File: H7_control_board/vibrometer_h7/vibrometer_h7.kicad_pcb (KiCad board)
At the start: 4 copper layers, 69.5 x 69.5 mm, 216 parts, among them J201 Conn_01x04_Socket, J204 TC2030-NL, J301 USB_C_Receptacle_USB2.0_16P, J501 debug_conn, J601 Conn_01x08_Socket, J701 Conn_01x08_Socket, J801 Conn_01x08_Socket, J901 PH-313D, Q1001 NMOS, Q1002 NMOS, Q1003 NMOS, Q201 BSS138, Q202 BSS138, Q203 BSS138, SW201 SW_Push, SW501 SW_Push, SW502 SW_Push, U201 STM32H723VGTx, U301 USBLC6-2SC6, U302 MT9700, U303 AMS1117-3V3, U901 RC4580, U902 TPA6111A2, Y201 24MHz

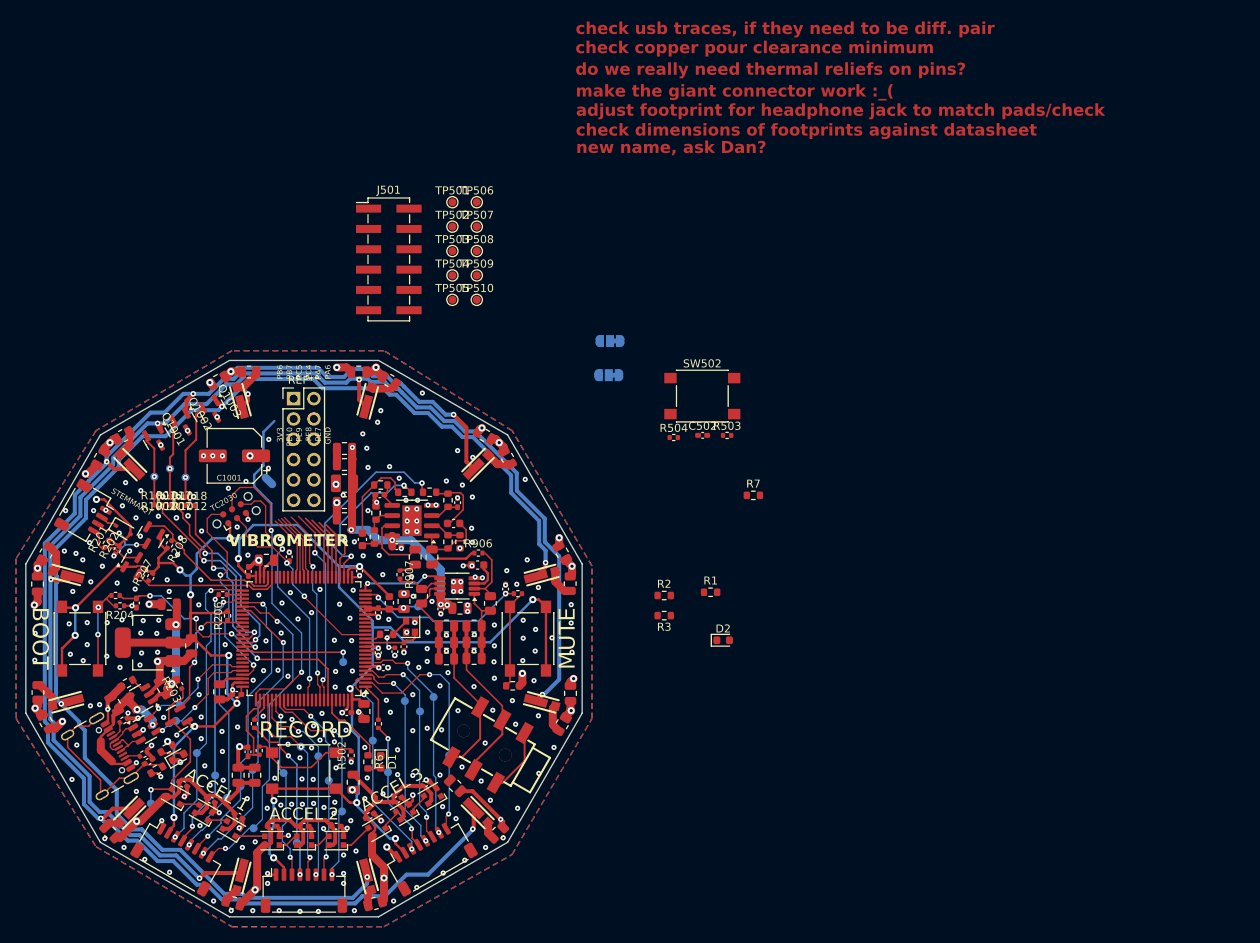
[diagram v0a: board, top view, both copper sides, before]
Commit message: some rerouting, cleaned up silkscreen
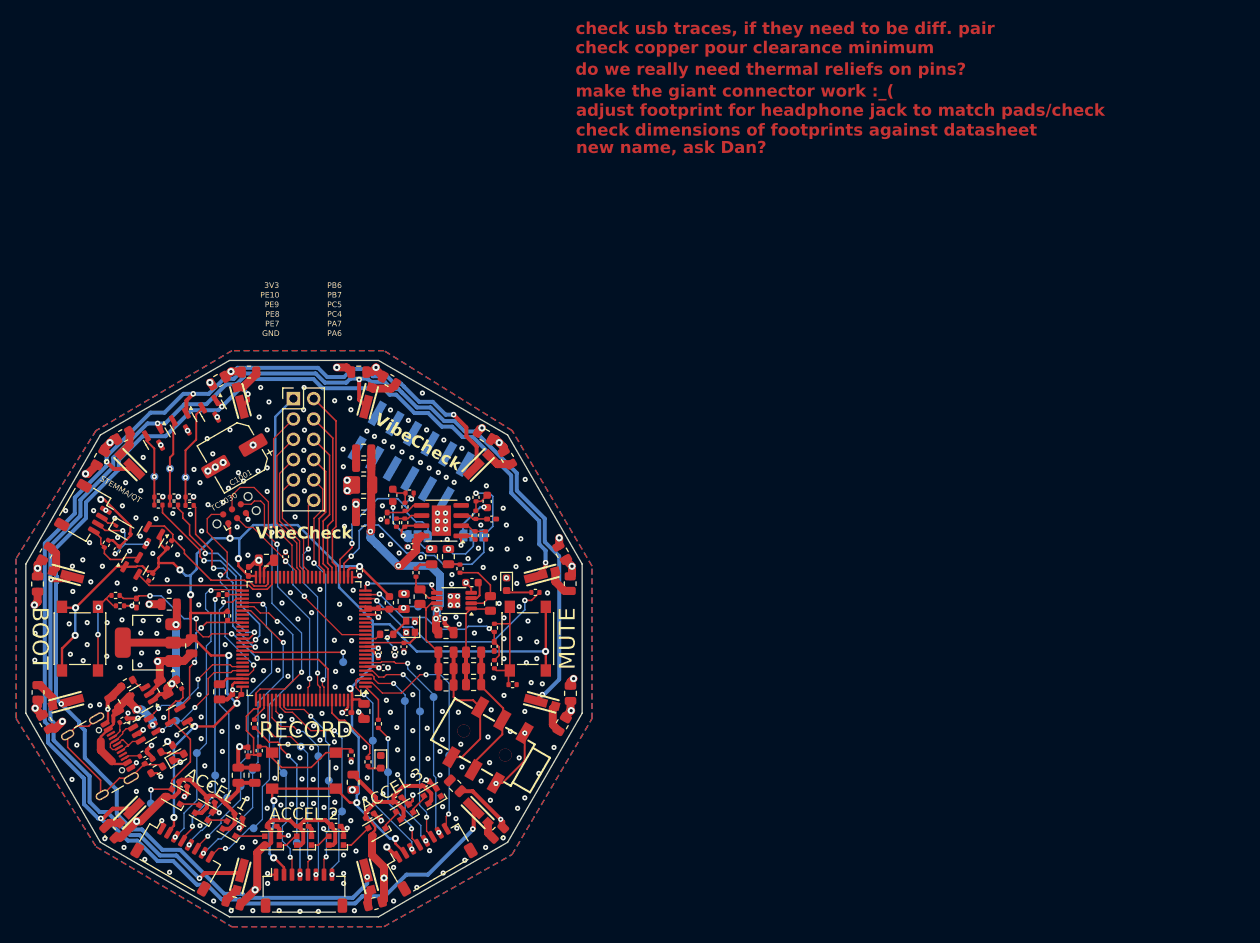
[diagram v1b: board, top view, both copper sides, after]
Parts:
- removed the C502 at (199.8, 74.6)
- removed the C502 at (175.2, 93.8)
- removed R1, R2, R3: 0, Resistor_SMD:R_0603_1608Metric
- removed the R504 at (196.2, 74.9)
- removed the R504 at (176.1, 105.9)
- removed REF**: PinHeader_2x06_P2.54mm_Vertical, Connector_PinHeader_2.54mm:PinHeader_2x06_P2.54mm_Vertical
- removed the SW502 at (199.8, 69.7)
- removed the SW502 at (178.0, 100.0)
- removed TP501, TP502, TP503, TP504, TP505, TP506, TP507, TP508, TP509, TP510: TestPoint, TestPoint:TestPoint_Pad_D1.0mm
- added C502: 100n, Capacitor_SMD:C_0402_1005Metric_Pad0.74x0.62mm_HandSolder, F.Cu at (173.8, 101.0)
- added J202: Conn_02x06, Connector_PinHeader_2.54mm:PinHeader_2x06_P2.54mm_Vertical, F.Cu at (148.7, 70.0)
- added R504: 10k, Resistor_SMD:R_0402_1005Metric, F.Cu at (176.1, 105.8)
- added SW502: SW_Push, Button_Switch_SMD:SW_SPST_PTS645, F.Cu at (178.0, 100.0)
- J501: moved to B.Cu
- R6, R7, R901, R902, R904, R905, R908, R909, R911, R912: footprint Resistor_SMD:R_0603_1608Metric -> Resistor_SMD:R_0402_1005Metric
- moved R503 37.7 mm to (173.8, 98.7), turned to -90 degrees
- moved JP901 31.3 mm to (164.2, 87.2), turned to 0 degrees
- moved R7 29.8 mm to (178.9, 94.2), turned to 180 degrees
- moved JP902 29.7 mm to (171.2, 87.1), turned to 0 degrees
- moved D2 28.0 mm to (175.3, 93.2), turned to -90 degrees
- moved J501 24.8 mm to (163.4, 77.2), turned to 60 degrees
- moved TP305 11.1 mm to (159.1, 88.2)
- moved R503 9.30 mm to (173.8, 103.2), turned to 90 degrees
- moved C912 6.69 mm to (161.1, 82.1)
- moved R901 5.83 mm to (171.5, 82.3), turned to -90 degrees
- moved C902 5.02 mm to (172.9, 82.8), turned to 90 degrees
- moved C905 4.72 mm to (173.4, 85.0), turned to 180 degrees
- moved R911 4.20 mm to (162.6, 85.5)
- moved R909 4.07 mm to (162.6, 83.5), turned to -90 degrees
- moved R902 3.93 mm to (171.5, 84.5)
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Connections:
- J501 pad 10: Net-(J501-Pin_10) -> unconnected-(J501-Pin_10-Pad10)
- J501 pad 11: Net-(J501-Pin_11) -> unconnected-(J501-Pin_11-Pad11)
- J501 pad 12: Net-(J501-Pin_12) -> unconnected-(J501-Pin_12-Pad12)
- J501 pad 3: Net-(J501-Pin_3) -> unconnected-(J501-Pin_3-Pad3)
- J501 pad 4: Net-(J501-Pin_4) -> unconnected-(J501-Pin_4-Pad4)
- J501 pad 5: Net-(J501-Pin_5) -> unconnected-(J501-Pin_5-Pad5)
- J501 pad 6: Net-(J501-Pin_6) -> unconnected-(J501-Pin_6-Pad6)
- J501 pad 7: Net-(J501-Pin_7) -> unconnected-(J501-Pin_7-Pad7)
- J501 pad 8: Net-(J501-Pin_8) -> unconnected-(J501-Pin_8-Pad8)
- J501 pad 9: Net-(J501-Pin_9) -> unconnected-(J501-Pin_9-Pad9)
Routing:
- net /MCU/MUTE_INDICATOR: track 0.00 -> 27.3 mm, vias 0 -> 2
- net +5V: track 176.3 -> 193.3 mm, vias 17 -> 22
- net /MCU/ADC2_INP: track 7.16 -> 23.9 mm
- net /MCU/ADC2_INN: track 7.49 -> 21.3 mm
- net /MCU/UART_CTS: track 8.23 -> 22.0 mm
- net /MCU/UART_RTS: track 8.34 -> 19.3 mm
- net /MCU/ADC1_INP: track 7.95 -> 18.6 mm
- net Net-(JP902-A): track 0.00 -> 9.78 mm, vias 0 -> 2
- net Net-(JP901-A): track 0.00 -> 9.37 mm, vias 0 -> 2
- net /AUDIO/DAC_OUTA: track 25.6 -> 34.9 mm
- net /AUDIO/AMP2_OUT: track 11.2 -> 2.57 mm, vias 0 -> 1
- net /AUDIO/AMP2_FILT: track 11.4 -> 2.97 mm
- net /MCU/UART_TX: track 8.48 -> 16.7 mm
- net /MCU/ADC1_INN: track 8.31 -> 15.9 mm
- net /MCU/UART_RX: track 8.69 -> 14.1 mm
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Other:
- board text added: "VibeCheck"
- board text removed: "VIBROMETER"

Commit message: working through drc errors
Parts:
- moved R906 0.69 mm to (170.1, 90.9)
- moved C915 0.40 mm to (171.0, 92.6)
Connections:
- U901 pad 9: (no net) -> unconnected-(U901-Pad9)
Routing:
- net /ACCEL/ACCEL.NCS1: track 37.5 -> 38.4 mm
- net Net-(C909-Pad2): track 1.47 -> 2.18 mm
- net GND: track 100.2 -> 100.6 mm, vias 342 -> 345
- net +5V: vias 22 -> 18

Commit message: nearly done....
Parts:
- added TP203: GPIO_timing1, TestPoint:TestPoint_Pad_D1.0mm, B.Cu at (154.2, 95.7)
- added TP204: GPIO_timing2, TestPoint:TestPoint_Pad_D1.0mm, B.Cu at (155.2, 97.9)
- C202, C203, C205, C207, C208, C209, C210, C211, C301, C308, C401, C402, C403, C404, C405, C406, C407, C408, C409, C501, C502, C901, C904: footprint Capacitor_SMD:C_0402_1005Metric_Pad0.74x0.62mm_HandSolder -> Capacitor_SMD:C_0402_1005Metric
- C306: footprint Capacitor_SMD:C_0805_2012Metric -> Capacitor_SMD:C_0603_1608Metric
- D1001, D1002, D1003, D1004, D1005, D1006, D1007, D1008, D1009, D1010, D1011, D1012: value LED -> LED_WHT
- D301: value LED -> LED_GRN
- D501: renamed from D1; value LED -> LED_RED
- D502: renamed from D2; value LED -> LED_RED
- Q1001, Q1002, Q1003: value NMOS -> NTR4170N
- R302: footprint Resistor_SMD:R_0603_1608Metric -> Resistor_SMD:R_0402_1005Metric
- U902: footprint Package_SO:HVSSOP-8-1EP_3x3mm_P0.65mm_EP1.57x1.89mm -> Package_SO:SOIC-8-1EP_3.9x4.9mm_P1.27mm_EP2.29x3mm
- moved C904 1.45 mm to (165.9, 98.5), turned to 180 degrees
- moved R906 1.20 mm to (169.7, 89.8)
- moved C915 1.03 mm to (170.6, 91.7)
- moved TP401 0.90 mm to (138.9, 116.2)
- moved C903 0.90 mm to (168.6, 99.0)
- moved R910 0.76 mm to (164.0, 95.3)
- moved TP302 0.70 mm to (134.0, 99.7)
- moved Q1002 0.47 mm to (135.1, 73.5), turned to 120 degrees
- moved R907 0.47 mm to (164.0, 91.3)
- moved L302 0.46 mm to (157.9, 80.8)
- moved Q1001 0.44 mm to (131.9, 75.3), turned to 120 degrees
- moved Q1003 0.44 mm to (138.2, 71.7), turned to 120 degrees
- moved C211 0.36 mm to (147.8, 90.1)
- moved C306 0.35 mm to (162.2, 95.5)
- moved TP402 0.26 mm to (149.1, 125.2)
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- renumbered R1003 to R1001, R1004 to R1002, R1005 to R1003, R1006 to R1004, R1008 to R1005, R1009 to R1006, R1010 to R1007, R1011 to R1008, R1013 to R1009, R1014 to R1010, R1015 to R1011, R1016 to R1012, R1001 to R1013, R1002 to R1014, R1017 to R1015, R1007 to R1016, R1018 to R1017, R1012 to R1018, R6 to R502, R502 to R503, R503 to R504, R7 to R505, R504 to R506
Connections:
- Q1001 pad 1: /STROBE/FET1_D -> Net-(Q1001-G)
- Q1001 pad 2: Net-(Q1001-G) -> GND
- Q1001 pad 3: GND -> /STROBE/FET1_D
- Q1002 pad 1: /STROBE/FET2_D -> Net-(Q1002-G)
- Q1002 pad 2: Net-(Q1002-G) -> GND
- Q1002 pad 3: GND -> /STROBE/FET2_D
- Q1003 pad 1: /STROBE/FET3_D -> Net-(Q1003-G)
- Q1003 pad 2: Net-(Q1003-G) -> GND
- Q1003 pad 3: GND -> /STROBE/FET3_D
- U201 pad 17: unconnected-(U201-PC2_C-Pad17) -> Net-(U201-PC2_C)
- U201 pad 22: unconnected-(U201-PA0-Pad22) -> Net-(U201-PA0)
- U901 pad 9: unconnected-(U901-Pad9) -> GND
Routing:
- net Net-(U201-PA0): track 0.00 -> 3.56 mm, vias 0 -> 1
- net GND: track 100.6 -> 97.1 mm, vias 345 -> 351
- net +5VA: track 36.1 -> 39.4 mm
- net Net-(U201-PC2_C): track 0.00 -> 2.52 mm, vias 0 -> 1
- net Net-(Q1001-G): track 9.05 -> 6.83 mm
- net /MCU/SWD_NRST: track 23.4 -> 25.4 mm
- net /MCU/SWD_CLK: track 38.1 -> 40.1 mm
- net Net-(Q1002-G): track 10.7 -> 9.10 mm
- net /STROBE/FET2_D: track 180.2 -> 178.9 mm
- net Net-(Q1003-G): track 13.1 -> 11.8 mm
- net +5V: track 193.3 -> 192.2 mm
- net /MCU/SWD_SWO: track 30.2 -> 31.2 mm
- net /AUDIO/LN_OUT1: track 12.3 -> 11.3 mm
- net /AUDIO/LN_IN1: track 8.97 -> 9.77 mm
- net /AUDIO/LN_BYPASS: track 3.26 -> 4.04 mm
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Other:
- board text added: "- do we really need thermal reliefs on pins?"
- board text added: "- make the giant connector work :_("
- board text added: "- new name, ask Dan?"
- board text added: "1"
- board text added: "12"
- board text added: "3V3A"
- board text added: "5V"
- board text added: "5VA"
- board text added: "AMP"
- board text added: "DAC"
- board text added: "DAC EXT TRG"
- board text added: "FILT"
- board text added: "GPIO"
- board text added: "HARRIS LAB BROWN UNIVERSITY 8/2024"
- board text added: "INTA1"
- board text added: "INTA2"
- board text added: "INTA3"
- board text added: "INTB1"
- board text added: "INTB2"
- board text added: "INTB3"
- board text added: "L"
- board text added: "LED1"
- board text added: "LED2"
- board text added: "LED3"
- board text added: "MISO1"
- board text added: "MISO2"
- board text added: "MISO3"
- board text added: "MOSI1"
- board text added: "MOSI2"
- board text added: "MOSI3"
- board text added: "NCS1"
- board text added: "NCS2"
- board text added: "NCS3"
- board text added: "PA0"
- board text added: "PC2_C"
- board text added: "R"
- board text added: "RGB LED"
- board text added: "SCK1"
- board text added: "SCK2"
- board text added: "SCK3"
- board text added: "USB+"
- board text added: "USB-"
- board text added: "V1.0"
- board text removed: "do we really need thermal reliefs on pins?"
- board text removed: "make the giant connector work :_("
- board text removed: "new name, ask Dan?"

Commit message: checked all footprints, made tiny daughterboard
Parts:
- R1001, R1002, R1003, R1004, R1005, R1006, R1007, R1008, R1009, R1010, R1011, R1012: value ?? -> 30
- R209: footprint Resistor_SMD:R_0603_1608Metric -> Resistor_SMD:R_0402_1005Metric
- Y201: footprint Crystal:Crystal_SMD_2016-4Pin_2.0x1.6mm -> Crystal:Crystal_SMD_3225-4Pin_3.2x2.5mm
- moved C213 4.09 mm to (160.5, 97.7), turned to 90 degrees
- moved C212 2.38 mm to (160.5, 99.7), turned to 90 degrees
- moved TP304 1.41 mm to (163.7, 94.7)
- moved R209 1.21 mm to (159.4, 98.7), turned to -90 degrees
- moved R910 0.71 mm to (164.0, 94.6)
- moved C306 0.65 mm to (162.1, 94.9)
- moved L301 0.65 mm to (160.6, 94.9)
- moved Y201 0.53 mm to (162.8, 98.6)
- moved R903 0.15 mm to (173.4, 95.6)
- moved C915 0.15 mm to (170.7, 91.8)
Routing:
- net GND: track 97.1 -> 99.9 mm, vias 351 -> 354
- net +3V3: track 264.3 -> 262.1 mm
- net Net-(C213-Pad1): track 4.98 -> 2.84 mm, vias 2 -> 0
- net /MCU/MUTE_BUTTON: track 22.4 -> 23.7 mm
- net +5VA: track 39.4 -> 38.7 mm
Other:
- board text added: "- adjust footprint for headphone jack to match pads/check"
- board text removed: "adjust footprint for headphone jack to match pads/check"

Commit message: finished analog filter, made a logo :)
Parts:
- added G***: LOGO, LOGO, F.Cu at (150.4, 85.9)
- added G***: LOGO, LOGO, F.Cu at (164.8, 74.2)
- added G***: LOGO, LOGO, B.Cu at (174.5, 98.1)
- added G***: LOGO, LOGO, B.Cu at (139.3, 95.4)
- added G***: LOGO, LOGO, B.Cu at (127.2, 86.2)
- C902: value C_Small -> 100n; footprint Capacitor_SMD:C_0603_1608Metric -> Capacitor_SMD:C_0402_1005Metric
- C905, C912, C916: value C_Small -> 100n
- JP901: value AMP2 FILT BYPASS -> FILT BYPASS 2
- JP902: value AMP1 FILT BYPASS -> FILT BYPASS 1
- R901, R902, R908, R909: value R_Small_US -> 80; footprint Resistor_SMD:R_0402_1005Metric -> Resistor_SMD:R_0603_1608Metric
- R904, R911: value R_Small_US -> 5k9; footprint Resistor_SMD:R_0402_1005Metric -> Resistor_SMD:R_0603_1608Metric
- R905, R912: value R_Small_US -> 10k
- moved R901 3.00 mm to (174.2, 83.7), turned to 180 degrees
- moved TP302 1.95 mm to (134.0, 101.7)
- moved R908 1.39 mm to (163.4, 80.4)
- moved R206 1.25 mm to (139.7, 98.1)
- moved R911 0.80 mm to (162.7, 86.3)
- moved R909 0.78 mm to (162.6, 82.8)
- moved C902 0.75 mm to (172.2, 82.5), turned to 180 degrees
- moved R402 0.67 mm to (143.2, 110.4)
- moved R904 0.53 mm to (171.8, 87.5)
- moved R902 0.40 mm to (171.9, 84.5)
- moved C916 0.38 mm to (160.3, 84.4)
- moved C912 0.35 mm to (161.1, 81.8)
- moved C905 0.30 mm to (173.8, 85.0)
- moved R905 0.30 mm to (173.0, 87.1)
- moved C501 0.28 mm to (142.7, 114.2)
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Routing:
- net GND: track 99.9 -> 90.0 mm, vias 354 -> 365
- net /AUDIO/DAC_OUTA: track 34.9 -> 33.0 mm
- net /MCU/BIG_RED_BUTTON: track 10.4 -> 11.7 mm
- net /STROBE/FET1_D: track 172.7 -> 171.6 mm
- net /AUDIO/DAC_OUTB: track 23.3 -> 24.4 mm
- net /MCU/SWD_SWO: track 31.2 -> 30.3 mm
- net Net-(JP902-A): track 9.23 -> 10.0 mm
- net /ACCEL/SPI ACCELEROMETER2/ACCEL_SCK: track 21.4 -> 22.1 mm
- net /AUDIO/AUDIO_L: track 17.9 -> 18.7 mm
- net /AUDIO/AMP2_FB: track 3.31 -> 3.92 mm
- net /MCU/SWD_CLK: track 40.1 -> 39.6 mm
- net +5V: track 192.2 -> 192.5 mm, vias 18 -> 19
